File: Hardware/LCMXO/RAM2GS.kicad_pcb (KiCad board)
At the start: 4 copper layers, 67.3 x 48.5 mm, 62 parts, among them J1 IIgs RAM Exp., J2 JTAG, U1 LCMXO256-TN100, U10 74LVC1G04GW, U11 AP2127K-1.2TRG1, U12 25F010, U2 W9812G6KH-6, U3 60M, U4 74AHCT245PW, U5 74LVC245APW, U6 74LVC245APW, U7 74LVC245APW, U8 AZ1117CH-3.3TRG1, U9 74LVC1G04GW

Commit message: 2.1?
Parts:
- added G***: LOGO, LOGO, F.Cu at (67.2, 95.2)
- added G***: LOGO, LOGO, F.Cu at (87.5, 95.0)
- D1: value White -> Amber
- R8: value 180 -> 220
- turned U10 to 90 degrees
- turned U11 to 0 degrees
- turned U2 to -90 degrees
- turned U9 to -90 degrees
- renumbered H5 to H3, H3 to H5
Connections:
- net /R~CAS~ renamed /R~{CAS}
- net /R~CS~ renamed /R~{CS}
- net /R~RAS~ renamed /R~{RAS}
- net /R~WE~ renamed /R~{WE}
- net /S~CS~ renamed /S~{CS}
- net /~CCAS~ renamed /~{CCAS}
- net /~CCAS~in renamed /~{CCAS}in
- net /~CRAS~ renamed /~{CRAS}
- net /~CRAS~in renamed /~{CRAS}in
- net /~CROMSEL~ renamed /~{CROMSEL}
- net /~CSEL~ renamed /~{CSEL}
- net /~FWE~ renamed /~{FWE}
- net /~WE~in renamed /~{WE}in
- J2 pad 10: Net-(J2-Pad10) -> unconnected-(J2-Pin_10-Pad10)
- J2 pad 8: Net-(J2-Pad8) -> unconnected-(J2-Pin_8-Pad8)
- J2 pad 9: Net-(J2-Pad9) -> unconnected-(J2-Pin_9-Pad9)
- U1 pad 11: Net-(U1-Pad11) -> unconnected-(U1-PL4C-Pad11)
- U1 pad 13: Net-(U1-Pad13) -> unconnected-(U1-PL4D-Pad13)
- U1 pad 36: Net-(U1-Pad36) -> unconnected-(U1-PB5B/PCLK2_1-Pad36)
- U1 pad 52: Net-(U1-Pad52) -> unconnected-(U1-PR11B-Pad52)
- U1 pad 54: Net-(U1-Pad54) -> unconnected-(U1-PR11A-Pad54)
- U1 pad 59: Net-(U1-Pad59) -> unconnected-(U1-PR9D-Pad59)
- U1 pad 9: Net-(U1-Pad9) -> unconnected-(U1-PL4A-Pad9)
- U10 pad 1: Net-(U10-Pad1) -> unconnected-(U10-NC-Pad1)
- U11 pad 4: Net-(U11-Pad4) -> unconnected-(U11-NC-Pad4)
- U9 pad 1: Net-(U9-Pad1) -> unconnected-(U9-NC-Pad1)
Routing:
- net /LED: track 21.5 -> 24.5 mm, vias 0 -> 2
- net GND: track 179.4 -> 179.7 mm, vias 209 -> 206
- net +3V3: vias 109 -> 108
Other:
- net class Default removed
- rule pad_to_mask_clearance: 0.075 -> 0.0762
- rule solder_mask_min_width: 0.1 -> 0.127
- board text added: "D21B"
- board text added: "JLCJLCJLCJLC"
- board text removed: "4201D"
- board text removed: "8 MB RAM"
- board text removed: "D20B"
- board text removed: "GW"
- board text removed: "Garrett’s Workshop"
- board text removed: "for Apple IIgs"

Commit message: RC 2.2
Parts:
- J2: footprint Connector:Tag-Connect_TC2050-IDC-FP_2x05_P1.27mm_Vertical -> stdpads:Tag-Connect_TC2050-IDC-FP_2x05_P1.27mm_Vertical
- U1: value LCMXO256-TN100 -> LCMXO256C-4TN100C
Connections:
- J1 pad 11: +5V -> 5VC
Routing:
- net +3V3: track 274.9 -> 278.7 mm
- net GND: track 179.7 -> 182.3 mm, vias 206 -> 208
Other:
- board text added: "D22B"
- board text removed: "D21B"

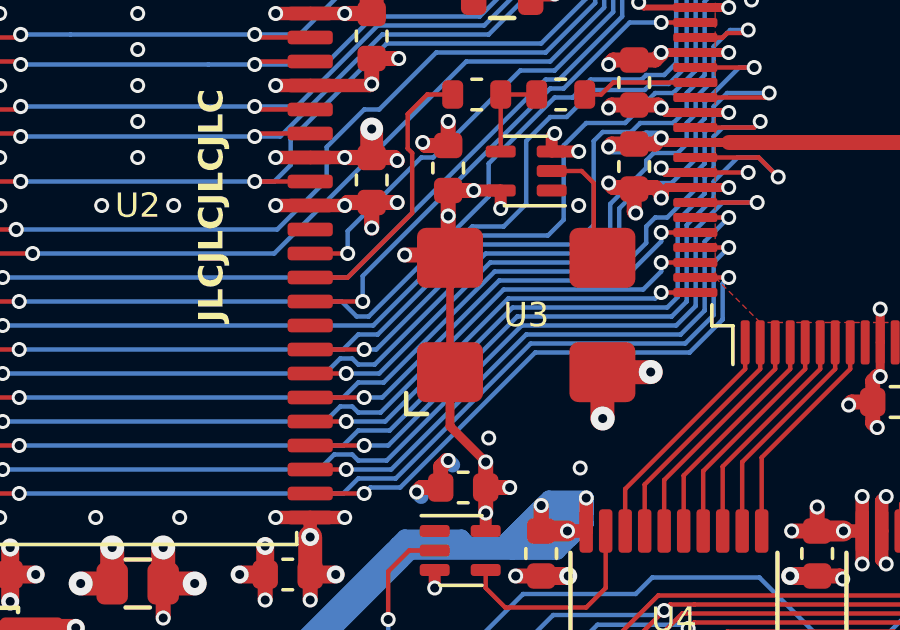
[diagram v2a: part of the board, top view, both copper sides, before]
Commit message: RC
Remove MachXO crystal oscillator EN jumper under keepout area
Remvoe DNP 3d models on MachXO2
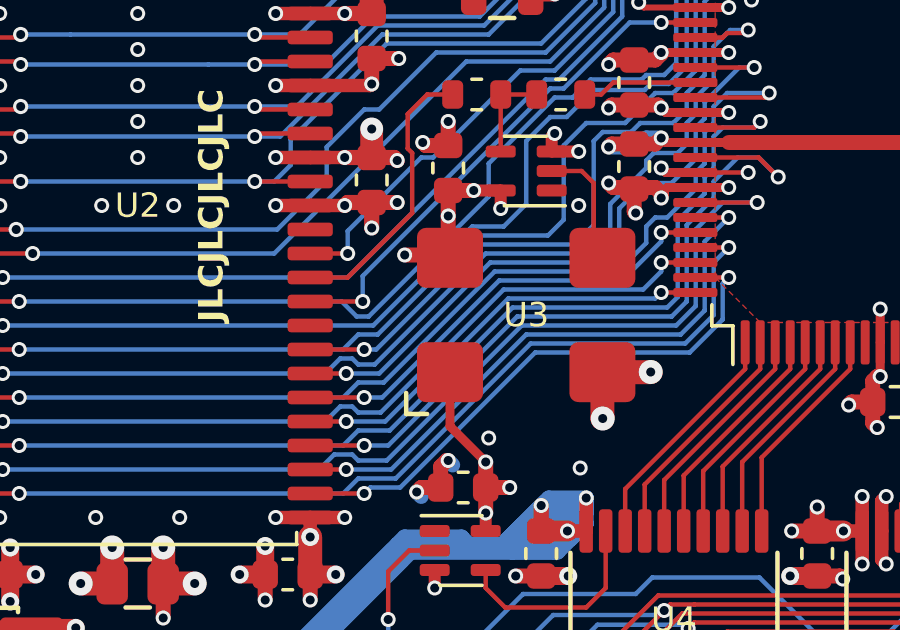
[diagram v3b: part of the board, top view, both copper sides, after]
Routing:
- net +3V3: track 278.7 -> 274.9 mm
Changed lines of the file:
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@@
   (segment (start 102.3 107.7) (end 102.3 108.15) (width 0.895) (layer "F.Cu") (net 37))
   (segment (start 79.36 104.55) (end 77.7375 104.55) (width 0.2) (layer "F.Cu") (net 37))
-  (segment (start 69.56 113.395) (end 69.56 117.205) (width 0.254) (layer "F.Cu") (net 37))
   (segment (start 100.3 106.15) (end 102.3 108.15) (width 1.524) (layer "F.Cu") (net 37))
   (segment (start 70.75 122.5) (end 70.75 121.9) (width 0.4) (layer "F.Cu") (net 37))

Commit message: RC
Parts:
- C30: value 15p -> 22p
- U1: value LCMXO256C-4TN100C -> LCMXO256C-3TN100C
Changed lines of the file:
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@@
       (polygon
         (pts
-          (xy 101.228936 100.067962)
-          (xy 104.821038 103.660064)
-          (xy 105.719064 102.762038)
-          (xy 102.126962 99.169936)
+          (xy 101.049331 100.067962)
+          (xy 104.821038 103.839669)
+          (xy 105.898669 102.762038)
+          (xy 102.126962 98.990331)
         )
       )
@@
     (descr "TQFP, 100 Pin (http://www.microsemi.com/index.php?option=com_docman&task=doc_download&gid=131095), generated with kicad-footprint-generator ipc_gullwing_generator.py")
     (tags "TQFP QFP")
-    (property "LCSC Part" "C1550734")
+    (property "LCSC Part" "C1521848")
     (property "Sheetfile" "RAM2GS.kicad_sch")
     (property "Sheetname" "")
@@
         (effects (font (size 0.8128 0.8128) (thickness 0.2032)))
     )
-    (fp_text value "LCMXO256C-4TN100C" (at 1.05 0 90) (layer "F.Fab")
+    (fp_text value "LCMXO256C-3TN100C" (at 1.05 0 90) (layer "F.Fab")
         (effects (font (size 0.508 0.508) (thickness 0.127)))
     )
@@
       (net 77 "/Ain9") (pinfunction "PR11D") (pintype "bidirectional"))
     (pad "52" smd roundrect (at 5.5 -7.6625 90) (size 1.475 0.3) (layers "F.Cu" "F.Paste" "F.Mask") (roundrect_rratio 0.25)
-      (net 119 "unconnected-(U1-PR11B-Pad52)") (pinfunction "PR11B") (pintype "bidirectional"))
+      (net 119 "unconnected-(U1-PR11B-Pad52)") (pinfunction "PR11B") (pintype "bidirectional+no_connect"))
     (pad "53" smd roundrect (at 5 -7.6625 90) (size 1.475 0.3) (layers "F.Cu" "F.Paste" "F.Mask") (roundrect_rratio 0.25)
       (net 112 "/S~{CS}") (pinfunction "PR11C") (pintype "bidirectional"))
     (pad "54" smd roundrect (at 4.5 -7.6625 90) (size 1.475 0.3) (layers "F.Cu" "F.Paste" "F.Mask") (roundrect_rratio 0.25)
-      (net 120 "unconnected-(U1-PR11A-Pad54)") (pinfunction "PR11A") (pintype "bidirectional"))
+      (net 120 "unconnected-(U1-PR11A-Pad54)") (pinfunction "PR11A") (pintype "bidirectional+no_connect"))
     (pad "55" smd roundrect (at 4 -7.6625 90) (size 1.475 0.3) (layers "F.Cu" "F.Paste" "F.Mask") (roundrect_rratio 0.25)
       (net 109 "/MISO") (pinfunction "PR10D") (pintype "bidirectional"))
@@
       (net 111 "/SCK") (pinfunction "PR10A") (pintype "bidirectional"))
     (pad "59" smd roundrect (at 2 -7.6625 90) (size 1.475 0.3) (layers "F.Cu" "F.Paste" "F.Mask") (roundrect_rratio 0.25)
-      (net 121 "unconnected-(U1-PR9D-Pad59)") (pinfunction "PR9D") (pintype "bidirectional"))
+      (net 121 "unconnected-(U1-PR9D-Pad59)") (pinfunction "PR9D") (pintype "bidirectional+no_connect"))
     (pad "60" smd roundrect (at 1.5 -7.6625 90) (size 1.475 0.3) (layers "F.Cu" "F.Paste" "F.Mask") (roundrect_rratio 0.25)
       (net 37 "+3V3") (pinfunction "VccIO1") (pintype "power_in"))
@@
         (effects (font (size 0.254 0.254) (thickness 0.0635)))
     )
-    (fp_text value "15p" (at 0 0.25 45) (layer "F.Fab")
+    (fp_text value "22p" (at 0 0.25 45) (layer "F.Fab")
         (effects (font (size 0.127 0.127) (thickness 0.03175)))
     )
@@
   (segment (start 108.65 110.35) (end 107.15 108.85) (width 1.524) (layer "B.Cu") (net 105))
   (segment (start 68.05 122.7) (end 69.95 122.7) (width 0.5) (layer "B.Cu") (net 105))
-  (segment (start 70.2 122.95) (end 70.95 122.95) (width 0.5) (layer "B.Cu") (net 105))
   (segment (start 73.15 123.2) (end 68.25 123.2) (width 0.508) (layer "B.Cu") (net 105))
   (segment (start 74.1 121.4) (end 73.475 122.025) (width 0.5) (layer "B.Cu") (net 105))
@@
   (segment (start 108.65 107.15) (end 107.5 106) (width 1.524) (layer "B.Cu") (net 105))
   (segment (start 70.2 122.95) (end 71.3 122.95) (width 0.5) (layer "B.Cu") (net 105))
+  (segment (start 70.2 122.95) (end 70.95 122.95) (width 0.5) (layer "B.Cu") (net 105))
   (segment (start 72.1 122.5) (end 73.475 122.5) (width 1) (layer "B.Cu") (net 105))
   (segment (start 60.198 130.556) (end 59.45 129.808) (width 1) (layer "B.Cu") (net 105))
@@
       )
     )
-  )
-  (zone (net 0) (net_name "") (layer "F.Cu") (hatch edge 0.508)
-    (connect_pads (clearance 0))
-    (min_thickness 0.254) (filled_areas_thickness no)
-    (keepout (tracks allowed) (vias allowed) (pads allowed) (copperpour not_allowed) (footprints allowed))
-    (fill (thermal_gap 0.508) (thermal_bridge_width 0.508))
-    (polygon
-      (pts
-        (xy 105.7219 102.76374)
-        (xy 104.82274 103.6629)
-        (xy 101.22864 100.0688)
-        (xy 102.1278 99.16964)
-      )
-    )

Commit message: 2.2
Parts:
- H1, H2, H3, H4, H5: value (none) -> ~
